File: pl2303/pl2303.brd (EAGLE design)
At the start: 3 parts, among them J1 ESP-STACK-HEADER, SW1 SW_TACT_2P-3X6

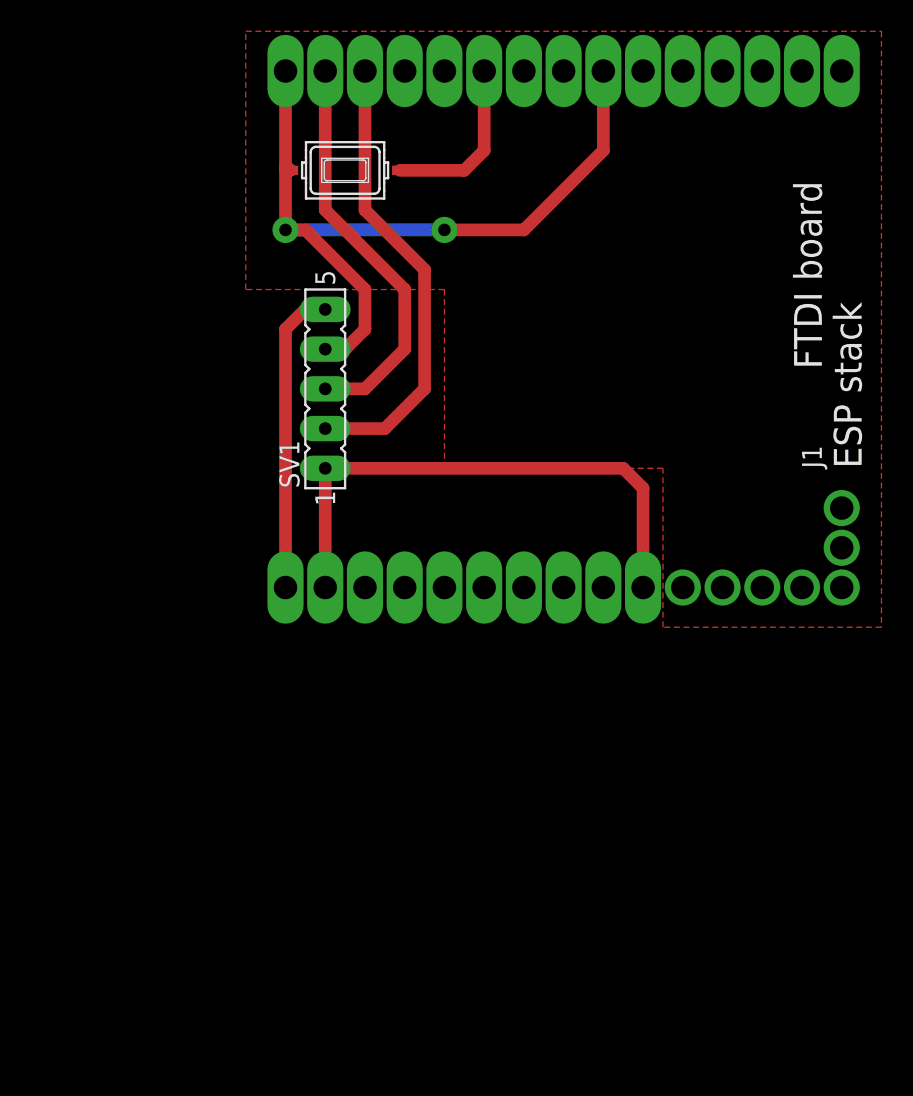
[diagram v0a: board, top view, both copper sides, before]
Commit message: FTDI board update - new board size and mounting holes
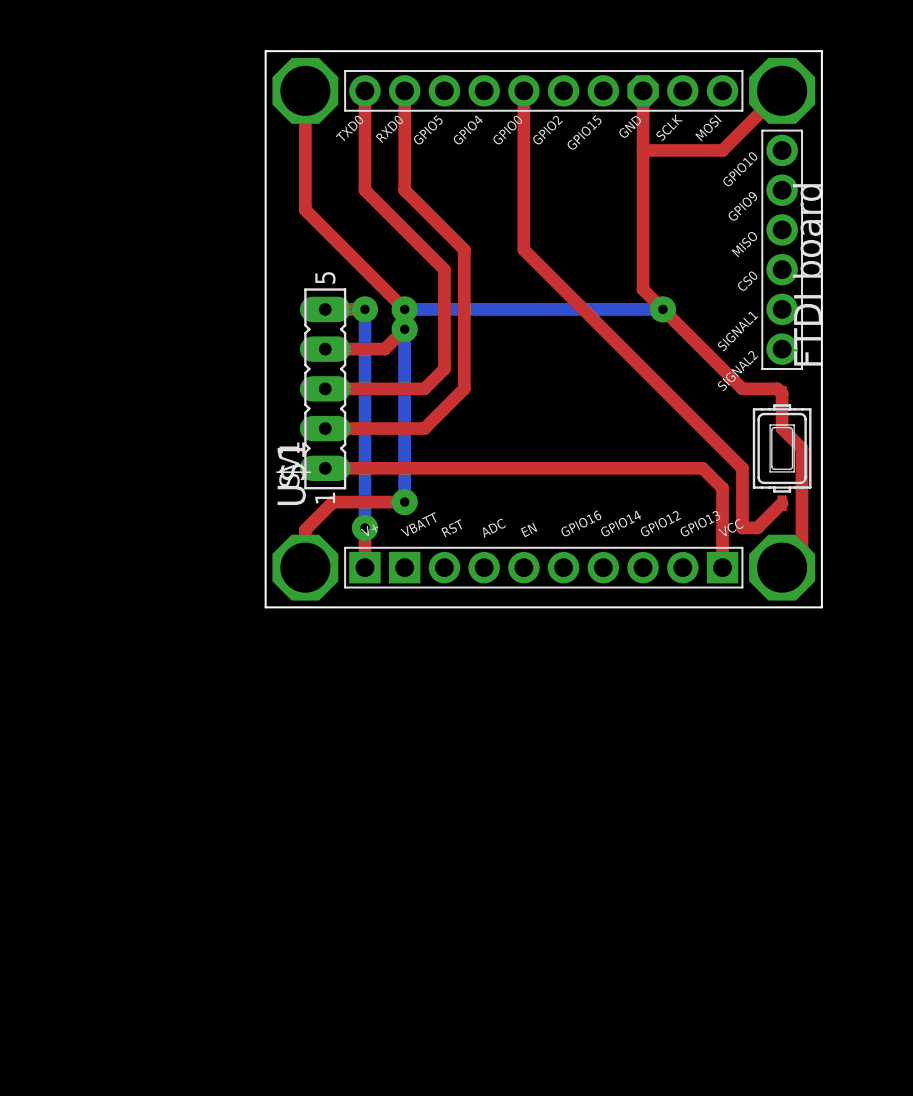
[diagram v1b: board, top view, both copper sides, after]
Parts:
- removed J1: ESP-STACK-HEADER, ESPstack:ESP-STACK-HEADER
- added U$1: ESP-BOARD, ESPstack:ESP-BOARD
- moved SW1 33.1 mm to (48.3, 40.6), turned to 270 degrees
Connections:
- new net VBATT: U$1.VBATT
- net +3V3: now also U$1.VCC; no longer J1.3V3@1, J1.3V3@2
- net +5V: now also U$1.V+; no longer J1.VBAT
- net GND: now also U$1.GND@1, U$1.GND@2, U$1.GND@3, U$1.GND@4, U$1.GND@5; no longer J1.GND@1, J1.GND@2
- net GPIO0: now also U$1.GPIO0; no longer J1.GPIO0
- net RXD0: now also U$1.RXD0; no longer J1.RXD0
- net TXD0: now also U$1.TXD0; no longer J1.TXD0
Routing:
- net GND: track 50.4 -> 107.5 mm, vias 2 -> 4
- net GPIO0: track 11.0 -> 36.9 mm
- net +3V3: track 34.8 -> 31.0 mm
- net TXD0: track 26.0 -> 28.0 mm
- net RXD0: track 29.3 -> 30.6 mm
- net +5V: track 19.6 -> 19.0 mm, vias 0 -> 2
- removed copper zone on layer 1, net GND
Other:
- board outline added: 35.6 x 35.6 mm
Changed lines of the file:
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@@
 <attribute name="MPN" value="" x="19.05" y="44.45" size="1.778" layer="27" rot="R90" display="off"/>
 </element>
-<element name="J1" library="ESPstack" package="ESP-STACK-HEADER" value="ESP-STACK-HEADER" x="26.67" y="48.26"/>
-<element name="SW1" library="dp_devices" package="SW_TACT_3X6" value="SW_TACT_2P-3X6" x="20.32" y="58.42"/>
+<element name="SW1" library="dp_devices" package="SW_TACT_3X6" value="SW_TACT_2P-3X6" x="48.26" y="40.64" rot="R270"/>
+<element name="U$1" library="ESPstack" package="ESP-BOARD" value="ESP-BOARD" x="39.37" y="49.53"/>
 </elements>
 <signals>
 <signal name="GND">
-<contactref element="J1" pad="GND@2"/>
-<contactref element="J1" pad="GND@1"/>
 <contactref element="SW1" pad="1"/>
 <contactref element="SV1" pad="4"/>
-<wire x1="16.51" y1="64.77" x2="16.51" y2="58.73" width="0.8128" layer="1"/>
-<wire x1="16.51" y1="58.73" x2="16.82" y2="58.42" width="0.8128" layer="1"/>
-<wire x1="36.83" y1="64.77" x2="36.83" y2="59.69" width="0.8128" layer="1"/>
-<wire x1="36.83" y1="59.69" x2="31.75" y2="54.61" width="0.8128" layer="1"/>
-<wire x1="31.75" y1="54.61" x2="26.67" y2="54.61" width="0.8128" layer="1"/>
-<via x="26.67" y="54.61" extent="1-16" drill="0.8" diameter="1.6764" shape="square"/>
-<wire x1="26.67" y1="54.61" x2="16.51" y2="54.61" width="0.8128" layer="16"/>
-<via x="16.51" y="54.61" extent="1-16" drill="0.8" diameter="1.6764" shape="square"/>
-<wire x1="16.51" y1="54.61" x2="16.51" y2="58.42" width="0.8128" layer="1"/>
-<wire x1="16.51" y1="58.42" x2="16.82" y2="58.42" width="0.8128" layer="1"/>
-<wire x1="19.05" y1="46.99" x2="20.32" y2="46.99" width="0.8128" layer="1"/>
-<wire x1="20.32" y1="46.99" x2="21.59" y2="48.26" width="0.8128" layer="1"/>
-<wire x1="21.59" y1="48.26" x2="21.59" y2="50.8" width="0.8128" layer="1"/>
-<wire x1="21.59" y1="50.8" x2="17.78" y2="54.61" width="0.8128" layer="1"/>
-<wire x1="17.78" y1="54.61" x2="16.51" y2="54.61" width="0.8128" layer="1"/>
-<polygon width="0.4064" layer="1" isolate="0.8128">
-<vertex x="13.97" y="67.31"/>
-<vertex x="54.61" y="67.31"/>
-<vertex x="54.61" y="29.21"/>
-<vertex x="40.64" y="29.21"/>
-<vertex x="40.64" y="39.37"/>
-<vertex x="26.67" y="39.37"/>
-<vertex x="26.67" y="50.8"/>
-<vertex x="13.97" y="50.8"/>
-</polygon>
+<contactref element="U$1" pad="GND@5"/>
+<contactref element="U$1" pad="GND@1"/>
+<contactref element="U$1" pad="GND@2"/>
+<contactref element="U$1" pad="GND@3"/>
+<contactref element="U$1" pad="GND@4"/>
+<wire x1="39.37" y1="63.5" x2="39.37" y2="59.69" width="0.8128" layer="1"/>
+<wire x1="39.37" y1="59.69" x2="39.37" y2="50.8" width="0.8128" layer="1"/>
+<wire x1="39.37" y1="50.8" x2="40.64" y2="49.53" width="0.8128" layer="1"/>
+<wire x1="45.72" y1="44.45" x2="47.95" y2="44.45" width="0.8128" layer="1"/>
+<wire x1="47.95" y1="44.45" x2="48.26" y2="44.14" width="0.8128" layer="1"/>
+<wire x1="48.26" y1="63.5" x2="44.45" y2="59.69" width="0.8128" layer="1"/>
+<wire x1="44.45" y1="59.69" x2="39.37" y2="59.69" width="0.8128" layer="1"/>
+<wire x1="48.26" y1="44.14" x2="48.26" y2="41.91" width="0.8128" layer="1"/>
+<wire x1="48.26" y1="41.91" x2="49.53" y2="40.64" width="0.8128" layer="1"/>
+<wire x1="49.53" y1="40.64" x2="49.53" y2="34.29" width="0.8128" layer="1"/>
+<wire x1="49.53" y1="34.29" x2="48.26" y2="33.02" width="0.8128" layer="1"/>
+<wire x1="17.78" y1="63.5" x2="17.78" y2="55.88" width="0.8128" layer="1"/>
+<wire x1="17.78" y1="55.88" x2="24.13" y2="49.53" width="0.8128" layer="1"/>
+<wire x1="17.78" y1="33.02" x2="17.78" y2="35.433" width="0.8128" layer="1"/>
+<wire x1="17.78" y1="35.433" x2="19.558" y2="37.211" width="0.8128" layer="1"/>
+<wire x1="19.05" y1="46.99" x2="22.86" y2="46.99" width="0.8128" layer="1"/>
+<wire x1="22.86" y1="46.99" x2="24.13" y2="48.26" width="0.8128" layer="1"/>
+<via x="24.13" y="49.53" extent="1-16" drill="0.6" diameter="1.6764" shape="octagon"/>
+<wire x1="24.13" y1="49.53" x2="40.64" y2="49.53" width="0.8128" layer="16"/>
+<via x="40.64" y="49.53" extent="1-16" drill="0.6" diameter="1.6764" shape="octagon"/>
+<wire x1="40.64" y1="49.53" x2="45.72" y2="44.45" width="0.8128" layer="1"/>
+<wire x1="19.558" y1="37.211" x2="24.13" y2="37.211" width="0.8128" layer="1"/>
+<via x="24.13" y="37.211" extent="1-16" drill="0.6" diameter="1.6764" shape="octagon"/>
+<wire x1="24.13" y1="37.211" x2="24.13" y2="48.26" width="0.8128" layer="16"/>
+<via x="24.13" y="48.26" extent="1-16" drill="0.6" diameter="1.6764" shape="octagon"/>
+<wire x1="24.13" y1="48.26" x2="24.13" y2="49.53" width="0.8128" layer="1"/>
 </signal>
 <signal name="+5V">
-<contactref element="J1" pad="VBAT"/>
 <contactref element="SV1" pad="5"/>
-<wire x1="16.51" y1="31.75" x2="16.51" y2="48.26" width="0.8128" layer="1"/>
-<wire x1="16.51" y1="48.26" x2="17.78" y2="49.53" width="0.8128" layer="1"/>
-<wire x1="17.78" y1="49.53" x2="19.05" y2="49.53" width="0.8128" layer="1"/>
+<contactref element="U$1" pad="V+"/>
+<wire x1="19.05" y1="49.53" x2="21.59" y2="49.53" width="0.8128" layer="1"/>
+<via x="21.59" y="49.53" extent="1-16" drill="0.6" diameter="1.6764"/>
+<wire x1="21.59" y1="49.53" x2="21.59" y2="35.56" width="0.8128" layer="16"/>
+<via x="21.59" y="35.56" extent="1-16" drill="0.6" diameter="1.6764" shape="square"/>
+<wire x1="21.59" y1="35.56" x2="21.59" y2="33.02" width="0.8128" layer="1"/>
 </signal>
 <signal name="+3V3">
-<contactref element="J1" pad="3V3@2"/>
-<contactref element="J1" pad="3V3@1"/>
 <contactref element="SV1" pad="1"/>
-<wire x1="19.05" y1="39.37" x2="19.05" y2="31.75" width="0.8128" layer="1"/>
-<wire x1="39.37" y1="31.75" x2="39.37" y2="38.1" width="0.8128" layer="1"/>
-<wire x1="39.37" y1="38.1" x2="38.1" y2="39.37" width="0.8128" layer="1"/>
-<wire x1="38.1" y1="39.37" x2="19.05" y2="39.37" width="0.8128" layer="1"/>
+<contactref element="U$1" pad="VCC"/>
+<wire x1="19.05" y1="39.37" x2="43.18" y2="39.37" width="0.8128" layer="1"/>
+<wire x1="43.18" y1="39.37" x2="44.45" y2="38.1" width="0.8128" layer="1"/>
+<wire x1="44.45" y1="38.1" x2="44.45" y2="33.02" width="0.8128" layer="1"/>
 </signal>
 <signal name="TXD0">
-<contactref element="J1" pad="TXD0"/>
 <contactref element="SV1" pad="3"/>
-<wire x1="19.05" y1="44.45" x2="21.59" y2="44.45" width="0.8128" layer="1"/>
-<wire x1="21.59" y1="44.45" x2="24.13" y2="46.99" width="0.8128" layer="1"/>
-<wire x1="24.13" y1="46.99" x2="24.13" y2="50.8" width="0.8128" layer="1"/>
-<wire x1="24.13" y1="50.8" x2="19.05" y2="55.88" width="0.8128" layer="1"/>
-<wire x1="19.05" y1="55.88" x2="19.05" y2="64.77" width="0.8128" layer="1"/>
+<contactref element="U$1" pad="TXD0"/>
+<wire x1="19.05" y1="44.45" x2="25.4" y2="44.45" width="0.8128" layer="1"/>
+<wire x1="25.4" y1="44.45" x2="26.67" y2="45.72" width="0.8128" layer="1"/>
+<wire x1="26.67" y1="45.72" x2="26.67" y2="52.07" width="0.8128" layer="1"/>
+<wire x1="26.67" y1="52.07" x2="21.59" y2="57.15" width="0.8128" layer="1"/>
+<wire x1="21.59" y1="57.15" x2="21.59" y2="63.5" width="0.8128" layer="1"/>
 </signal>
 <signal name="RXD0">
-<contactref element="J1" pad="RXD0"/>
 <contactref element="SV1" pad="2"/>
-<wire x1="19.05" y1="41.91" x2="22.86" y2="41.91" width="0.8128" layer="1"/>
-<wire x1="22.86" y1="41.91" x2="25.4" y2="44.45" width="0.8128" layer="1"/>
-<wire x1="25.4" y1="44.45" x2="25.4" y2="52.07" width="0.8128" layer="1"/>
-<wire x1="25.4" y1="52.07" x2="21.59" y2="55.88" width="0.8128" layer="1"/>
-<wire x1="21.59" y1="55.88" x2="21.59" y2="64.77" width="0.8128" layer="1"/>
+<contactref element="U$1" pad="RXD0"/>
+<wire x1="24.13" y1="63.5" x2="24.13" y2="57.15" width="0.8128" layer="1"/>
+<wire x1="24.13" y1="57.15" x2="27.94" y2="53.34" width="0.8128" layer="1"/>
+<wire x1="27.94" y1="53.34" x2="27.94" y2="44.45" width="0.8128" layer="1"/>
+<wire x1="27.94" y1="44.45" x2="25.4" y2="41.91" width="0.8128" layer="1"/>
+<wire x1="25.4" y1="41.91" x2="19.05" y2="41.91" width="0.8128" layer="1"/>
 </signal>
 <signal name="N$1">
 </signal>
 <signal name="GPIO0">
-<contactref element="J1" pad="GPIO0"/>
 <contactref element="SW1" pad="2"/>
-<wire x1="23.82" y1="58.42" x2="27.94" y2="58.42" width="0.8128" layer="1"/>
-<wire x1="27.94" y1="58.42" x2="29.21" y2="59.69" width="0.8128" layer="1"/>
-<wire x1="29.21" y1="59.69" x2="29.21" y2="64.77" width="0.8128" layer="1"/>
+<contactref element="U$1" pad="GPIO0"/>
+<wire x1="31.75" y1="63.5" x2="31.75" y2="53.34" width="0.8128" layer="1"/>
+<wire x1="31.75" y1="53.34" x2="45.72" y2="39.37" width="0.8128" layer="1"/>
+<wire x1="45.72" y1="39.37" x2="45.72" y2="35.56" width="0.8128" layer="1"/>
+<wire x1="45.72" y1="35.56" x2="46.68" y2="35.56" width="0.8128" layer="1"/>
+<wire x1="46.68" y1="35.56" x2="48.26" y2="37.14" width="0.8128" layer="1"/>
+</signal>
+<signal name="VBATT">
+<contactref element="U$1" pad="VBATT"/>
 </signal>
 </signals>

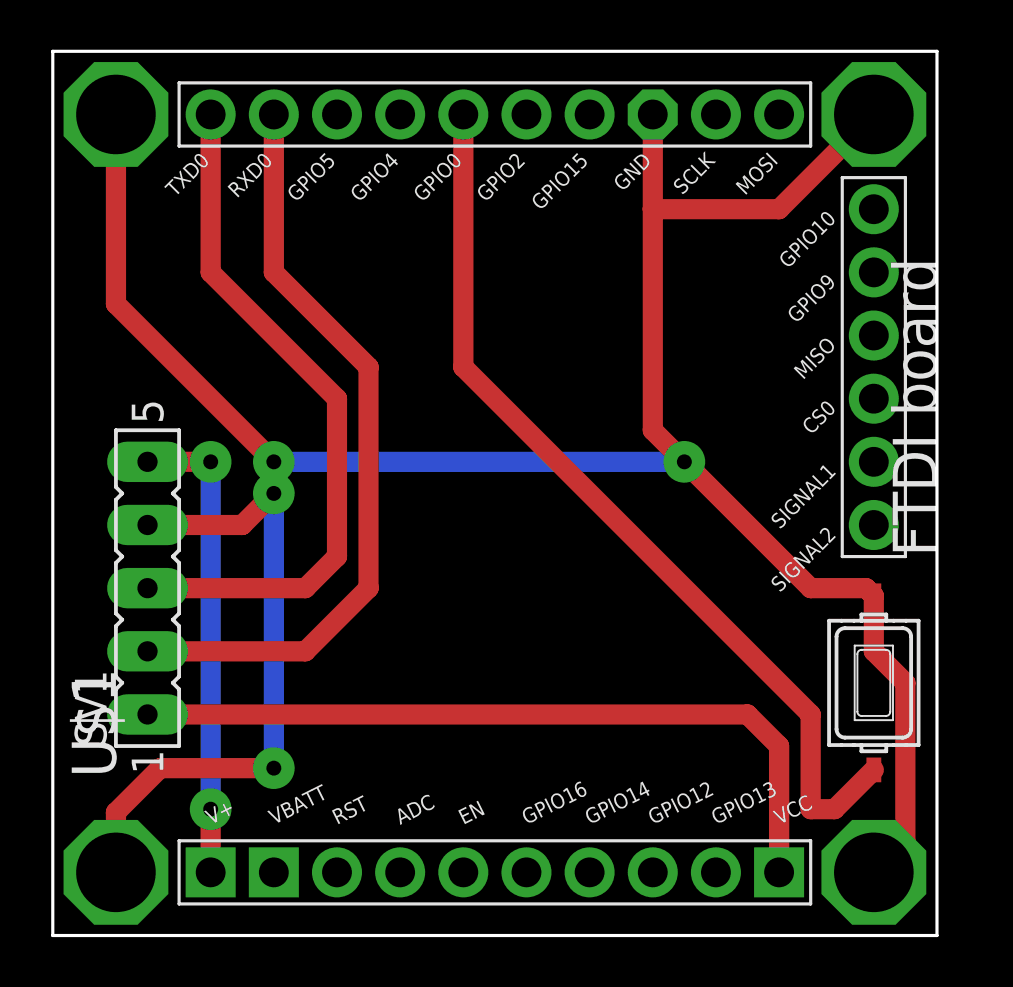
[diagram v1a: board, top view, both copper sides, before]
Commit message: Small clearance improvements, bigger header pads and mounting holes
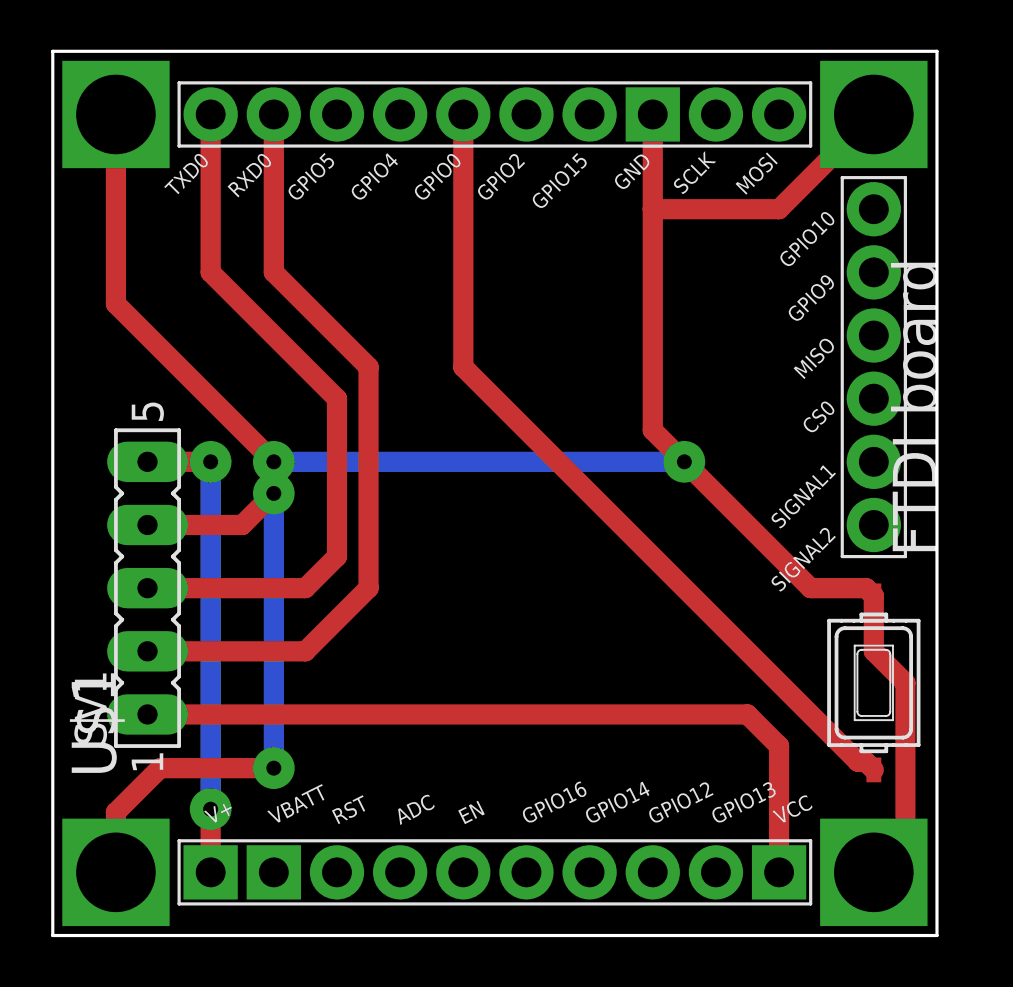
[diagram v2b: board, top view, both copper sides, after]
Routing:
- net GPIO0: track 36.9 -> 33.4 mm
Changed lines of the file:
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@@
 <contactref element="U$1" pad="GPIO0"/>
 <wire x1="31.75" y1="63.5" x2="31.75" y2="53.34" width="0.8128" layer="1"/>
-<wire x1="31.75" y1="53.34" x2="45.72" y2="39.37" width="0.8128" layer="1"/>
-<wire x1="45.72" y1="39.37" x2="45.72" y2="35.56" width="0.8128" layer="1"/>
-<wire x1="45.72" y1="35.56" x2="46.68" y2="35.56" width="0.8128" layer="1"/>
-<wire x1="46.68" y1="35.56" x2="48.26" y2="37.14" width="0.8128" layer="1"/>
+<wire x1="31.75" y1="53.34" x2="47.625" y2="37.465" width="0.8128" layer="1"/>
+<wire x1="47.625" y1="37.465" x2="47.935" y2="37.465" width="0.8128" layer="1"/>
+<wire x1="47.935" y1="37.465" x2="48.26" y2="37.14" width="0.8128" layer="1"/>
 </signal>
 <signal name="VBATT">
